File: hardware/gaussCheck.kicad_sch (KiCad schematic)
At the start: 17 parts, among them J1 USB_C_Receptacle_USB2.0, SW2 PT847S, SW3 PT847S, SW4 PT847S, U1 TLV493D, U2 VIM-878-DP

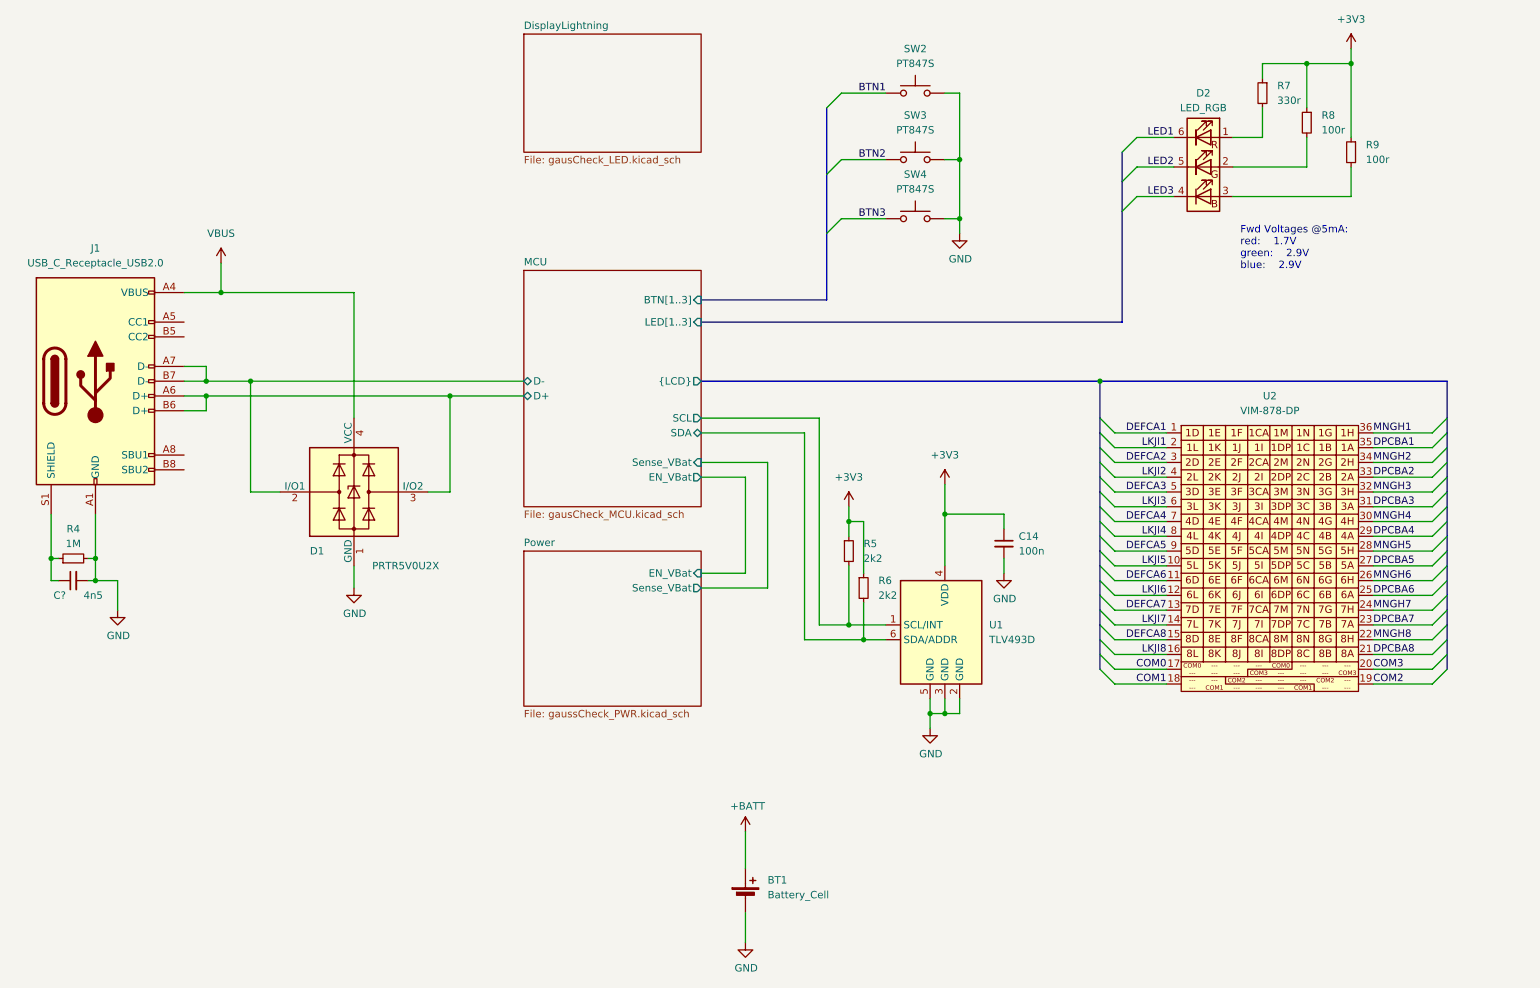
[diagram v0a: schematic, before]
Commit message: custom LED daughter board for display lightning added resistors to USB-C CC line
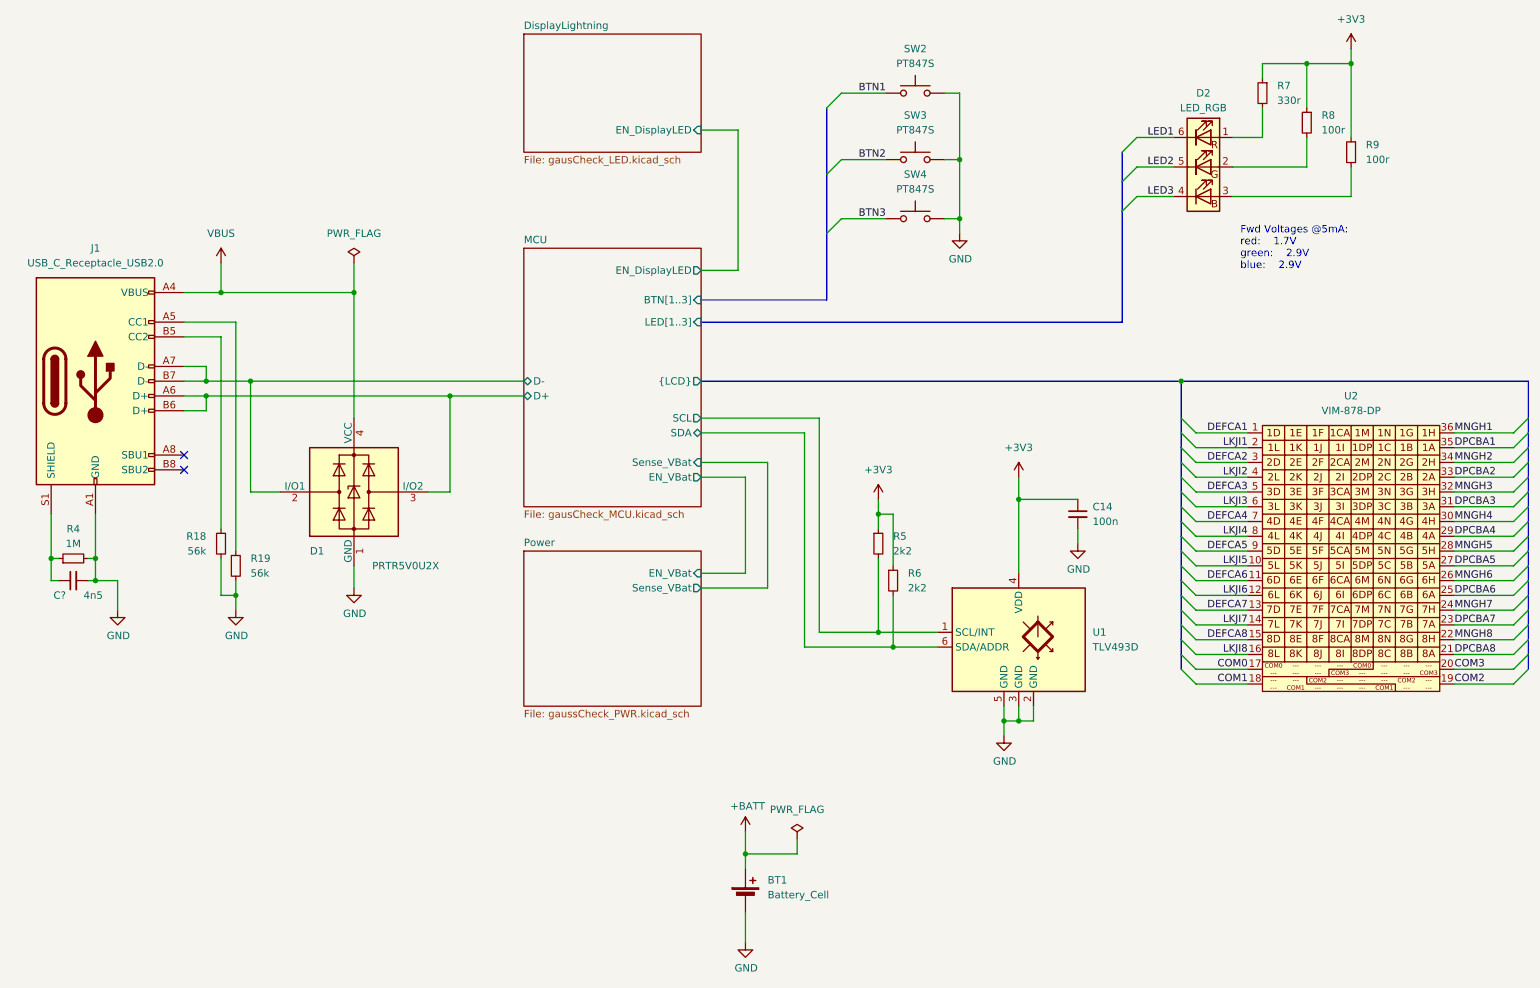
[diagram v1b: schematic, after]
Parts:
- added R18, R19: 56k, Resistor_SMD:R_0603_1608Metric, symbol Device:R_Small
- U1: symbol Sensor_Magnetic:TLV493D -> GaussCheckCustomSymbols:TLV493D
- U2: MPN VIM-878-DP-RC-S-LV -> VIM-878-DP-FC-S-LV
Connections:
- net GND: now also R18.2, R19.2
- net at J1.A5 (CC1): now also R19.1
- net at J1.B5 (CC2): now also R18.1
- no-connect marks 0 -> 2
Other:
- sheet DisplayLightning ports: added EN_DisplayLED; removed none
- sheet MCU ports: added EN_DisplayLED; removed none
- moved on the sheet: C14, R5, R6, U2

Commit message: update Mouser Nr..
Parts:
- BT1: Mouser (none) -> 534-3034
- C14: MPN (none) -> C0603C104K9RACTU; Mouser (none) -> 80-C0603C104K9R
- C?: MPN (none) -> C0603Y471K9RACTU; Mouser (none) -> 80-C0603Y471K9R
- D1: MPN PRTR5V0U2X -> PRTR5V0U2X-QR; Mouser (none) -> 771-PRTR5V0U2X-QR
- D2: Mouser (none) -> 941-P6CFKBCKNPRGJ7A3
- J1: Mouser (none) -> 640-USB4105-GF-A
- R18, R19: MPN (none) -> CRCW060356K0FKEAC; Mouser (none) -> 71-CRCW060356K0FKEAC
- R4: MPN (none) -> CRCW06031M00FKED; Mouser (none) -> 71-CRCW06031M00FKED
- R5, R6: MPN (none) -> CRCW06032K20JNEA; Mouser (none) -> 71-CRCW0603J-2.2K-E3
- R7: MPN (none) -> CRCW0603330RFKEC; Mouser (none) -> 71-CRCW0603330RFKEC
- R8, R9: MPN (none) -> CRCW0603100RJNEC; Mouser (none) -> 71-CRCW0603100RJNEC
- SW2, SW3, SW4: Mouser (none) -> 611-PTS847350SMTR2LF
- U1: Mouser (none) -> 726-TLV493DA1B6HTSA2
- U2: MPN VIM-878-DP-FC-S-LV -> VIM-878-DP-RC-S-LV; Mouser (none) -> 825-VIM878DPRCSLV
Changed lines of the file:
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@@
+      (effects (font (size 1.27 1.27)) hide)
+    )
+    (property "MPN" "CRCW060356K0FKEAC" (at 49.53 116.84 0)
+      (effects (font (size 1.27 1.27)) hide)
+    )
+    (property "Mouser" "71-CRCW060356K0FKEAC" (at 49.53 116.84 0)
       (effects (font (size 1.27 1.27)) hide)
     )
@@
       (effects (font (size 1.27 1.27)) hide)
     )
+    (property "Mouser" "611-PTS847350SMTR2LF" (at 168.91 39.37 0)
+      (effects (font (size 1.27 1.27)) hide)
+    )
     (pin "1")
     (pin "2")
@@
     )
     (property "Datasheet" "~" (at 24.13 119.38 0)
+      (effects (font (size 1.27 1.27)) hide)
+    )
+    (property "MPN" "CRCW06031M00FKED" (at 24.13 119.38 0)
+      (effects (font (size 1.27 1.27)) hide)
+    )
+    (property "Mouser" "71-CRCW06031M00FKED" (at 24.13 119.38 0)
       (effects (font (size 1.27 1.27)) hide)
     )
@@
       (effects (font (size 1.27 1.27)) hide)
     )
+    (property "MPN" "CRCW0603100RJNEC" (at 236.22 44.45 0)
+      (effects (font (size 1.27 1.27)) hide)
+    )
+    (property "Mouser" "71-CRCW0603100RJNEC" (at 236.22 44.45 0)
+      (effects (font (size 1.27 1.27)) hide)
+    )
     (pin "1")
     (pin "2")
@@
       (effects (font (size 1.27 1.27)) hide)
     )
+    (property "MPN" "CRCW0603100RJNEC" (at 243.84 49.53 0)
+      (effects (font (size 1.27 1.27)) hide)
+    )
+    (property "Mouser" "71-CRCW0603100RJNEC" (at 243.84 49.53 0)
+      (effects (font (size 1.27 1.27)) hide)
+    )
     (pin "1")
     (pin "2")
@@
     )
     (property "Datasheet" "~" (at 52.07 120.65 0)
+      (effects (font (size 1.27 1.27)) hide)
+    )
+    (property "MPN" "CRCW060356K0FKEAC" (at 52.07 120.65 0)
+      (effects (font (size 1.27 1.27)) hide)
+    )
+    (property "Mouser" "71-CRCW060356K0FKEAC" (at 52.07 120.65 0)
       (effects (font (size 1.27 1.27)) hide)
     )
@@
     )
     (property "MPN" "CLP6C-FKB-CKNPRGJBB7a363" (at 218.44 52.07 0)
+      (effects (font (size 1.27 1.27)) hide)
+    )
+    (property "Mouser" "941-P6CFKBCKNPRGJ7A3" (at 218.44 52.07 0)
       (effects (font (size 1.27 1.27)) hide)
     )
@@
       (effects (font (size 1.27 1.27)) hide)
     )
-    (property "MPN" "VIM-878-DP-FC-S-LV" (at 243.84 119.38 0)
+    (property "MPN" "VIM-878-DP-RC-S-LV" (at 243.84 119.38 0)
+      (effects (font (size 1.27 1.27)) hide)
+    )
+    (property "Mouser" "825-VIM878DPRCSLV" (at 243.84 119.38 0)
       (effects (font (size 1.27 1.27)) hide)
     )
@@
       (effects (font (size 1.27 1.27)) hide)
     )
+    (property "Mouser" "726-TLV493DA1B6HTSA2" (at 186.69 134.62 0)
+      (effects (font (size 1.27 1.27)) hide)
+    )
     (pin "1")
     (pin "2")
@@
       (effects (font (size 1.27 1.27)) hide)
     )
+    (property "MPN" "CRCW06032K20JNEA" (at 162.56 116.84 0)
+      (effects (font (size 1.27 1.27)) hide)
+    )
+    (property "Mouser" "71-CRCW0603J-2.2K-E3" (at 162.56 116.84 0)
+      (effects (font (size 1.27 1.27)) hide)
+    )
     (pin "1")
     (pin "2")
@@
     )
     (property "DIGIKEY" "2073-USB4105-GF-ACT-ND" (at 27.94 88.9 0)
+      (effects (font (size 1.27 1.27)) hide)
+    )
+    (property "Mouser" "640-USB4105-GF-A" (at 27.94 88.9 0)
       (effects (font (size 1.27 1.27)) hide)
     )
@@
       (effects (font (size 1.27 1.27)) hide)
     )
+    (property "Mouser" "611-PTS847350SMTR2LF" (at 168.91 50.8 0)
+      (effects (font (size 1.27 1.27)) hide)
+    )
     (pin "1")
     (pin "2")
@@
       (effects (font (size 1.27 1.27)) hide)
     )
+    (property "Mouser" "534-3034" (at 139.7 177.8 0)
+      (effects (font (size 1.27 1.27)) hide)
+    )
     (pin "1")
     (pin "2")
@@
       (effects (font (size 1.27 1.27)) hide)
     )
-    (property "MPN" "PRTR5V0U2X" (at 72.39 107.95 0)
+    (property "MPN" "PRTR5V0U2X-QR" (at 72.39 107.95 0)
+      (effects (font (size 1.27 1.27)) hide)
+    )
+    (property "Mouser" "771-PRTR5V0U2X-QR" (at 72.39 107.95 0)
       (effects (font (size 1.27 1.27)) hide)
     )
@@
     )
     (property "Datasheet" "~" (at 24.13 123.19 0)
+      (effects (font (size 1.27 1.27)) hide)
+    )
+    (property "MPN" "C0603Y471K9RACTU" (at 24.13 123.19 0)
+      (effects (font (size 1.27 1.27)) hide)
+    )
+    (property "Mouser" "80-C0603Y471K9R" (at 24.13 123.19 0)
       (effects (font (size 1.27 1.27)) hide)
     )
@@
       (effects (font (size 1.27 1.27)) hide)
     )
+    (property "MPN" "CRCW06032K20JNEA" (at 165.1 123.19 0)
+      (effects (font (size 1.27 1.27)) hide)
+    )
+    (property "Mouser" "71-CRCW0603J-2.2K-E3" (at 165.1 123.19 0)
+      (effects (font (size 1.27 1.27)) hide)
+    )
     (pin "1")
     (pin "2")
@@
       (effects (font (size 1.27 1.27)) hide)
     )
+    (property "MPN" "C0603C104K9RACTU" (at 196.85 111.76 0)
+      (effects (font (size 1.27 1.27)) hide)
+    )
+    (property "Mouser" "80-C0603C104K9R" (at 196.85 111.76 0)
+      (effects (font (size 1.27 1.27)) hide)
+    )
     (pin "1")
     (pin "2")
@@
       (effects (font (size 1.27 1.27)) hide)
     )
+    (property "Mouser" "611-PTS847350SMTR2LF" (at 168.91 60.96 0)
+      (effects (font (size 1.27 1.27)) hide)
+    )
     (pin "1")
     (pin "2")
@@
       (effects (font (size 1.27 1.27)) hide)
     )
+    (property "MPN" "CRCW0603330RFKEC" (at 228.6 39.37 0)
+      (effects (font (size 1.27 1.27)) hide)
+    )
+    (property "Mouser" "71-CRCW0603330RFKEC" (at 228.6 39.37 0)
+      (effects (font (size 1.27 1.27)) hide)
+    )
